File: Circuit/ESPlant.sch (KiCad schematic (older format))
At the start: 43 parts, among them P1 SOIL, P101 CONN_DIGITAL, P102 CONN_ANALOG, P103 CONN_SERIAL, P104 CONN_I2C, P105 SOLAR, P106 USB_5PIN_SHELL, P109 CONN_PWR, P110 CONN_01X05, P111 UV, P112 TEMP, P113 NEOPIXEL, P114 PIR, Q101 FDN340P, SW101 RESET, SW102 PRGM, SW103 RESET, U101 STM32F042F, U103 ESP-12E

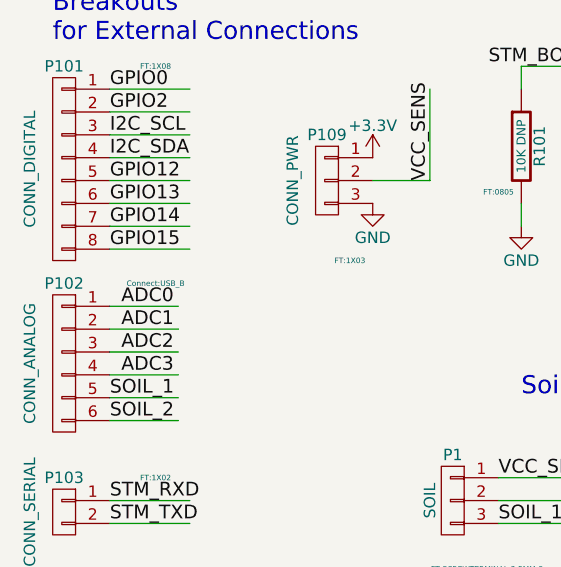
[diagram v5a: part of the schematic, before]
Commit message: First cut routing
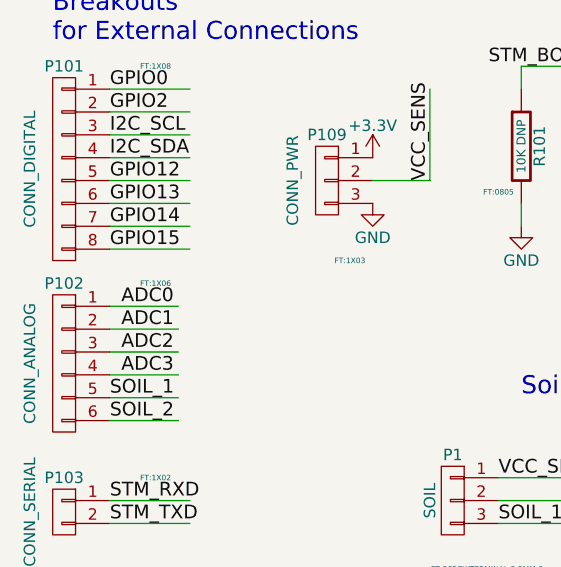
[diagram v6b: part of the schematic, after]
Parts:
- P102: footprint Connect:USB_B -> FT:1X06
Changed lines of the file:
@@
 F 0 "P102" H 750 6300 50  0000 C CNN
 F 1 "CONN_ANALOG" V 900 5950 50  0000 C CNN
-F 2 "Connect:USB_B" H 350 6300 24  0000 C CNN
+F 2 "FT:1X06" H 350 6300 24  0000 C CNN
 F 3 "" H 750 5950 60  0000 C CNN
 	1    750  5950

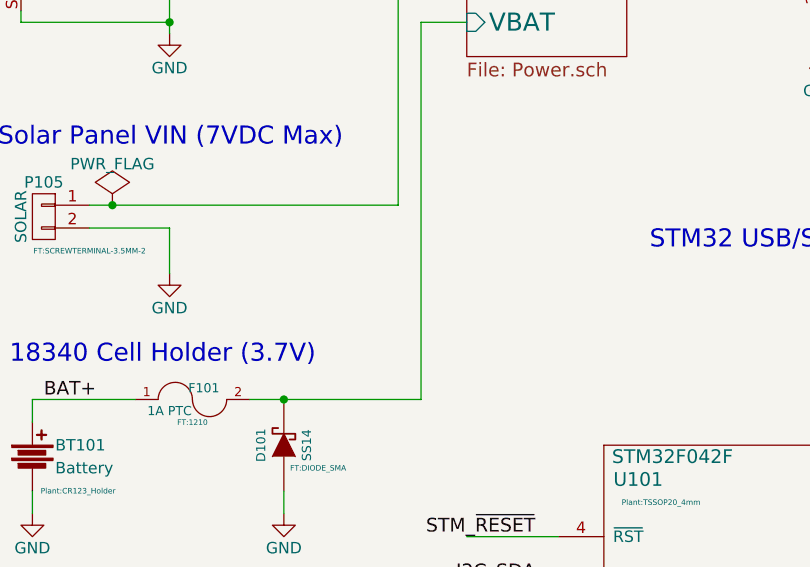
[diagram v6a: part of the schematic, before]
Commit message: Add crowbar diode for solar panel polarity protection
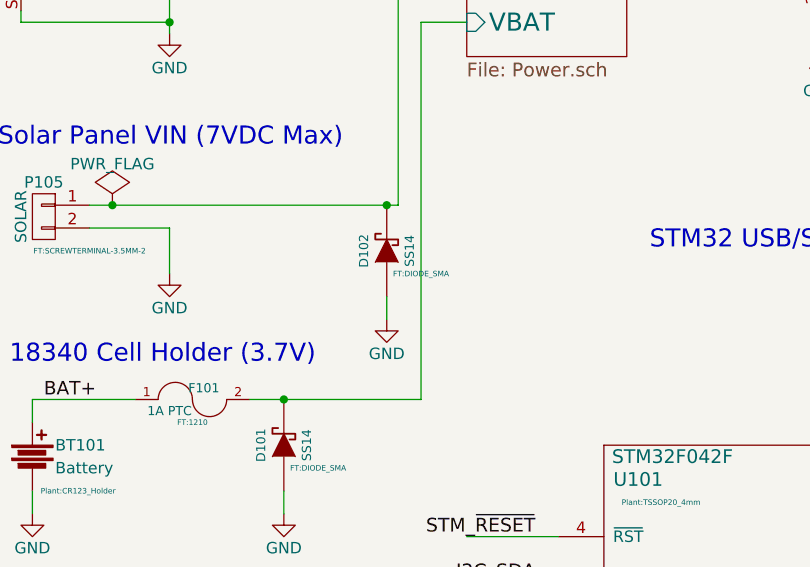
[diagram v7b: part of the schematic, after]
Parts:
- added D102: SS14, FT:DIODE_SMA, symbol DIODE_SCHOTTKY
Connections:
- wire segments 163 -> 164
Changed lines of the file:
@@
 $EndDescr
 $Comp
-L +3.3V #PWR01
+L +3.3V #PWR123
 U 1 1 56375ED2
 P 9250 5800
-F 0 "#PWR01" H 9250 5650 50  0001 C CNN
+F 0 "#PWR123" H 9250 5650 50  0001 C CNN
 F 1 "+3.3V" H 9250 5940 50  0000 C CNN
 F 2 "" H 9250 5800 60  0000 C CNN
@@
 $EndComp
 $Comp
-L GND #PWR02
+L GND #PWR129
 U 1 1 56375FE4
 P 10550 1700
-F 0 "#PWR02" H 10550 1450 50  0001 C CNN
+F 0 "#PWR129" H 10550 1450 50  0001 C CNN
 F 1 "GND" H 10550 1550 50  0000 C CNN
 F 2 "" H 10550 1700 60  0000 C CNN
@@
 $EndComp
 $Comp
-L +3.3V #PWR03
+L +3.3V #PWR128
 U 1 1 56376117
 P 10250 1400
-F 0 "#PWR03" H 10250 1250 50  0001 C CNN
+F 0 "#PWR128" H 10250 1250 50  0001 C CNN
 F 1 "+3.3V" H 10250 1540 50  0000 C CNN
 F 2 "" H 10250 1400 60  0000 C CNN
@@
 $EndComp
 $Comp
-L +3.3V #PWR04
+L +3.3V #PWR117
 U 1 1 5637689F
 P 7000 1800
-F 0 "#PWR04" H 7000 1650 50  0001 C CNN
+F 0 "#PWR117" H 7000 1650 50  0001 C CNN
 F 1 "+3.3V" H 7000 1950 50  0000 C CNN
 F 2 "" H 7000 1800 60  0000 C CNN
@@
 $EndComp
 $Comp
-L GND #PWR05
+L GND #PWR125
 U 1 1 5637692A
 P 9750 1950
-F 0 "#PWR05" H 9750 1700 50  0001 C CNN
+F 0 "#PWR125" H 9750 1700 50  0001 C CNN
 F 1 "GND" V 9750 1750 50  0000 C CNN
 F 2 "" H 9750 1950 60  0000 C CNN
@@
 $EndComp
 $Comp
-L GND #PWR06
+L GND #PWR102
 U 1 1 56377AB6
 P 1450 1600
-F 0 "#PWR06" H 1450 1350 50  0001 C CNN
+F 0 "#PWR102" H 1450 1350 50  0001 C CNN
 F 1 "GND" H 1450 1450 50  0000 C CNN
 F 2 "" H 1450 1600 60  0000 C CNN
@@
 $EndComp
 $Comp
-L GND #PWR07
+L GND #PWR121
 U 1 1 564A2882
 P 8900 6250
-F 0 "#PWR07" H 8900 6000 50  0001 C CNN
+F 0 "#PWR121" H 8900 6000 50  0001 C CNN
 F 1 "GND" H 8900 6100 50  0000 C CNN
 F 2 "" H 8900 6250 60  0000 C CNN
@@
 Solar Panel VIN (7VDC Max)
 $Comp
-L GND #PWR08
+L GND #PWR103
 U 1 1 564B24B3
 P 1450 2650
-F 0 "#PWR08" H 1450 2400 50  0001 C CNN
+F 0 "#PWR103" H 1450 2400 50  0001 C CNN
 F 1 "GND" H 1450 2500 50  0000 C CNN
 F 2 "" H 1450 2650 60  0000 C CNN
@@
 $EndComp
 $Comp
-L +3.3V #PWR09
+L +3.3V #PWR114
 U 1 1 564B2FF9
 P 5250 900
-F 0 "#PWR09" H 5250 750 50  0001 C CNN
+F 0 "#PWR114" H 5250 750 50  0001 C CNN
 F 1 "+3.3V" H 5250 1040 50  0000 C CNN
 F 2 "" H 5250 900 60  0000 C CNN
@@
 $EndComp
 $Comp
-L GND #PWR010
+L GND #PWR110
 U 1 1 564B3125
 P 4300 1700
-F 0 "#PWR010" H 4300 1450 50  0001 C CNN
+F 0 "#PWR110" H 4300 1450 50  0001 C CNN
 F 1 "GND" H 4300 1550 50  0000 C CNN
 F 2 "" H 4300 1700 60  0000 C CNN
@@
 18340 Cell Holder (3.7V)\n
 $Comp
-L GND #PWR011
+L GND #PWR101
 U 1 1 564B5F41
 P 850 3700
-F 0 "#PWR011" H 850 3450 50  0001 C CNN
+F 0 "#PWR101" H 850 3450 50  0001 C CNN
 F 1 "GND" H 850 3550 50  0000 C CNN
 F 2 "" H 850 3700 60  0000 C CNN
@@
 STM_~RESET
 $Comp
-L GND #PWR012
+L GND #PWR127
 U 1 1 564C3A22
 P 10200 5050
-F 0 "#PWR012" H 10200 4800 50  0001 C CNN
+F 0 "#PWR127" H 10200 4800 50  0001 C CNN
 F 1 "GND" H 10200 4900 50  0000 C CNN
 F 2 "" H 10200 5050 60  0000 C CNN
@@
 ESP_~RESET
 $Comp
-L GND #PWR013
+L GND #PWR124
 U 1 1 564C33B9
 P 9600 5050
-F 0 "#PWR013" H 9600 4800 50  0001 C CNN
+F 0 "#PWR124" H 9600 4800 50  0001 C CNN
 F 1 "GND" H 9600 4900 50  0000 C CNN
 F 2 "" H 9600 5050 60  0000 C CNN
@@
 STM_~RESET
 $Comp
-L GND #PWR014
+L GND #PWR130
 U 1 1 564C4984
 P 10700 5050
-F 0 "#PWR014" H 10700 4800 50  0001 C CNN
+F 0 "#PWR130" H 10700 4800 50  0001 C CNN
 F 1 "GND" H 10700 4900 50  0000 C CNN
 F 2 "" H 10700 5050 60  0000 C CNN
@@
 VCC_SENS
 $Comp
-L GND #PWR015
+L GND #PWR108
 U 1 1 564FA125
 P 2650 7350
-F 0 "#PWR015" H 2650 7100 50  0001 C CNN
+F 0 "#PWR108" H 2650 7100 50  0001 C CNN
 F 1 "GND" H 2650 7200 50  0000 C CNN
 F 2 "" H 2650 7350 60  0000 C CNN
@@
 ADC3
 $Comp
-L PWR_FLAG #FLG016
+L PWR_FLAG #FLG101
 U 1 1 5650A161
 P 1200 2350
-F 0 "#FLG016" H 1200 2445 50  0001 C CNN
+F 0 "#FLG101" H 1200 2445 50  0001 C CNN
 F 1 "PWR_FLAG" H 1200 2530 50  0000 C CNN
 F 2 "" H 1200 2350 60  0000 C CNN
@@
 $EndComp
 $Comp
-L GND #PWR017
+L GND #PWR116
 U 1 1 564E839D
 P 6700 5500
-F 0 "#PWR017" H 6700 5250 50  0001 C CNN
+F 0 "#PWR116" H 6700 5250 50  0001 C CNN
 F 1 "GND" H 6700 5350 50  0000 C CNN
 F 2 "" H 6700 5500 60  0000 C CNN
@@
 STM_SWCLK
 $Comp
-L GND #PWR018
+L GND #PWR112
 U 1 1 564EA3B7
 P 4550 5300
-F 0 "#PWR018" H 4550 5050 50  0001 C CNN
+F 0 "#PWR112" H 4550 5050 50  0001 C CNN
 F 1 "GND" H 4550 5150 50  0000 C CNN
 F 2 "" H 4550 5300 60  0000 C CNN
@@
 $EndComp
 $Comp
-L +3.3V #PWR019
+L +3.3V #PWR111
 U 1 1 564EA803
 P 4450 2800
-F 0 "#PWR019" H 4450 2650 50  0001 C CNN
+F 0 "#PWR111" H 4450 2650 50  0001 C CNN
 F 1 "+3.3V" H 4450 2940 50  0000 C CNN
 F 2 "" H 4450 2800 60  0000 C CNN
@@
 $EndComp
 $Comp
-L GND #PWR020
+L GND #PWR109
 U 1 1 564EB5A8
 P 2750 5350
-F 0 "#PWR020" H 2750 5100 50  0001 C CNN
+F 0 "#PWR109" H 2750 5100 50  0001 C CNN
 F 1 "GND" H 2750 5200 50  0000 C CNN
 F 2 "" H 2750 5350 60  0000 C CNN
@@
 $EndComp
 $Comp
-L +3.3V #PWR021
+L +3.3V #PWR118
 U 1 1 564ED1D2
 P 7400 5550
-F 0 "#PWR021" H 7400 5400 50  0001 C CNN
+F 0 "#PWR118" H 7400 5400 50  0001 C CNN
 F 1 "+3.3V" H 7400 5690 50  0000 C CNN
 F 2 "" H 7400 5550 60  0000 C CNN
@@
 $EndComp
 $Comp
-L GND #PWR022
+L GND #PWR119
 U 1 1 564ED428
 P 7400 6100
-F 0 "#PWR022" H 7400 5850 50  0001 C CNN
+F 0 "#PWR119" H 7400 5850 50  0001 C CNN
 F 1 "GND" H 7400 5950 50  0000 C CNN
 F 2 "" H 7400 6100 60  0000 C CNN
@@
 $EndComp
 $Comp
-L GND #PWR023
+L GND #PWR113
 U 1 1 564EE0F6
 P 5150 3250
-F 0 "#PWR023" H 5150 3000 50  0001 C CNN
+F 0 "#PWR113" H 5150 3000 50  0001 C CNN
 F 1 "GND" H 5150 3100 50  0001 C CNN
 F 2 "" H 5150 3250 60  0000 C CNN
@@
 $EndComp
 $Comp
-L GND #PWR024
+L GND #PWR120
 U 1 1 56576EBF
 P 8250 3600
-F 0 "#PWR024" H 8250 3350 50  0001 C CNN
+F 0 "#PWR120" H 8250 3350 50  0001 C CNN
 F 1 "GND" H 8250 3450 50  0000 C CNN
 F 2 "" H 8250 3600 60  0000 C CNN
@@
 $EndComp
 $Comp
-L GND #PWR025
+L GND #PWR131
 U 1 1 5657CEA4
 P 10800 3600
-F 0 "#PWR025" H 10800 3350 50  0001 C CNN
+F 0 "#PWR131" H 10800 3350 50  0001 C CNN
 F 1 "GND" H 10800 3450 50  0000 C CNN
 F 2 "" H 10800 3600 60  0000 C CNN
@@
 $EndComp
 $Comp
-L GND #PWR026
+L GND #PWR122
 U 1 1 5657D68A
 P 9050 3600
-F 0 "#PWR026" H 9050 3350 50  0001 C CNN
+F 0 "#PWR122" H 9050 3350 50  0001 C CNN
 F 1 "GND" H 9050 3450 50  0000 C CNN
 F 2 "" H 9050 3600 60  0000 C CNN
@@
 $EndComp
 $Comp
-L GND #PWR027
+L GND #PWR126
 U 1 1 5657D767
 P 9950 3600
-F 0 "#PWR027" H 9950 3350 50  0001 C CNN
+F 0 "#PWR126" H 9950 3350 50  0001 C CNN
 F 1 "GND" H 9950 3450 50  0000 C CNN
 F 2 "" H 9950 3600 60  0000 C CNN
@@
 $EndComp
 $Comp
-L +3.3V #PWR028
+L +3.3V #PWR115
 U 1 1 56596CF8
 P 6550 2350
-F 0 "#PWR028" H 6550 2200 50  0001 C CNN
+F 0 "#PWR115" H 6550 2200 50  0001 C CNN
 F 1 "+3.3V" H 6550 2490 50  0000 C CNN
 F 2 "" H 6550 2350 60  0000 C CNN
@@
 $EndComp
 $Comp
-L +3.3V #PWR029
+L +3.3V #PWR105
 U 1 1 565C1114
 P 2100 5050
-F 0 "#PWR029" H 2100 4900 50  0001 C CNN
+F 0 "#PWR105" H 2100 4900 50  0001 C CNN
 F 1 "+3.3V" H 2100 5190 50  0000 C CNN
 F 2 "" H 2100 5050 60  0000 C CNN
@@
 $EndComp
 $Comp
-L GND #PWR030
+L GND #PWR106
 U 1 1 565C1810
 P 2100 5250
-F 0 "#PWR030" H 2100 5000 50  0001 C CNN
+F 0 "#PWR106" H 2100 5000 50  0001 C CNN
 F 1 "GND" H 2100 5100 50  0000 C CNN
 F 2 "" H 2100 5250 60  0000 C CNN
@@
 $EndComp
 $Comp
-L GND #PWR031
+L GND #PWR104
 U 1 1 565D25EB
 P 1950 3700
-F 0 "#PWR031" H 1950 3450 50  0001 C CNN
+F 0 "#PWR104" H 1950 3450 50  0001 C CNN
 F 1 "GND" H 1950 3550 50  0000 C CNN
 F 2 "" H 1950 3700 60  0000 C CNN
@@
 GPIO14
 Connection ~ 1950 3200
+$Comp
+L DIODE_SCHOTTKY D102
+U 1 1 565BCCC2
+P 2400 2550
+F 0 "D102" H 2400 2650 40  0000 C CNN
+F 1 "SS14" H 2400 2450 40  0000 C CNN
+F 2 "FT:DIODE_SMA" V 2300 2400 24  0000 C CNN
+F 3 "" H 2400 2550 60  0000 C CNN
+	1    2400 2550
+	0    -1   -1   0
+$EndComp
+$Comp
+L GND #PWR107
+U 1 1 565BCCC8
+P 2400 2850
+F 0 "#PWR107" H 2400 2600 50  0001 C CNN
+F 1 "GND" H 2400 2700 50  0000 C CNN
+F 2 "" H 2400 2850 60  0000 C CNN
+F 3 "" H 2400 2850 60  0000 C CNN
+	1    2400 2850
+	1    0    0    -1
+$EndComp
+Wire Wire Line
+	2400 2750 2400 2850
+Connection ~ 2400 2350
 $EndSCHEMATC

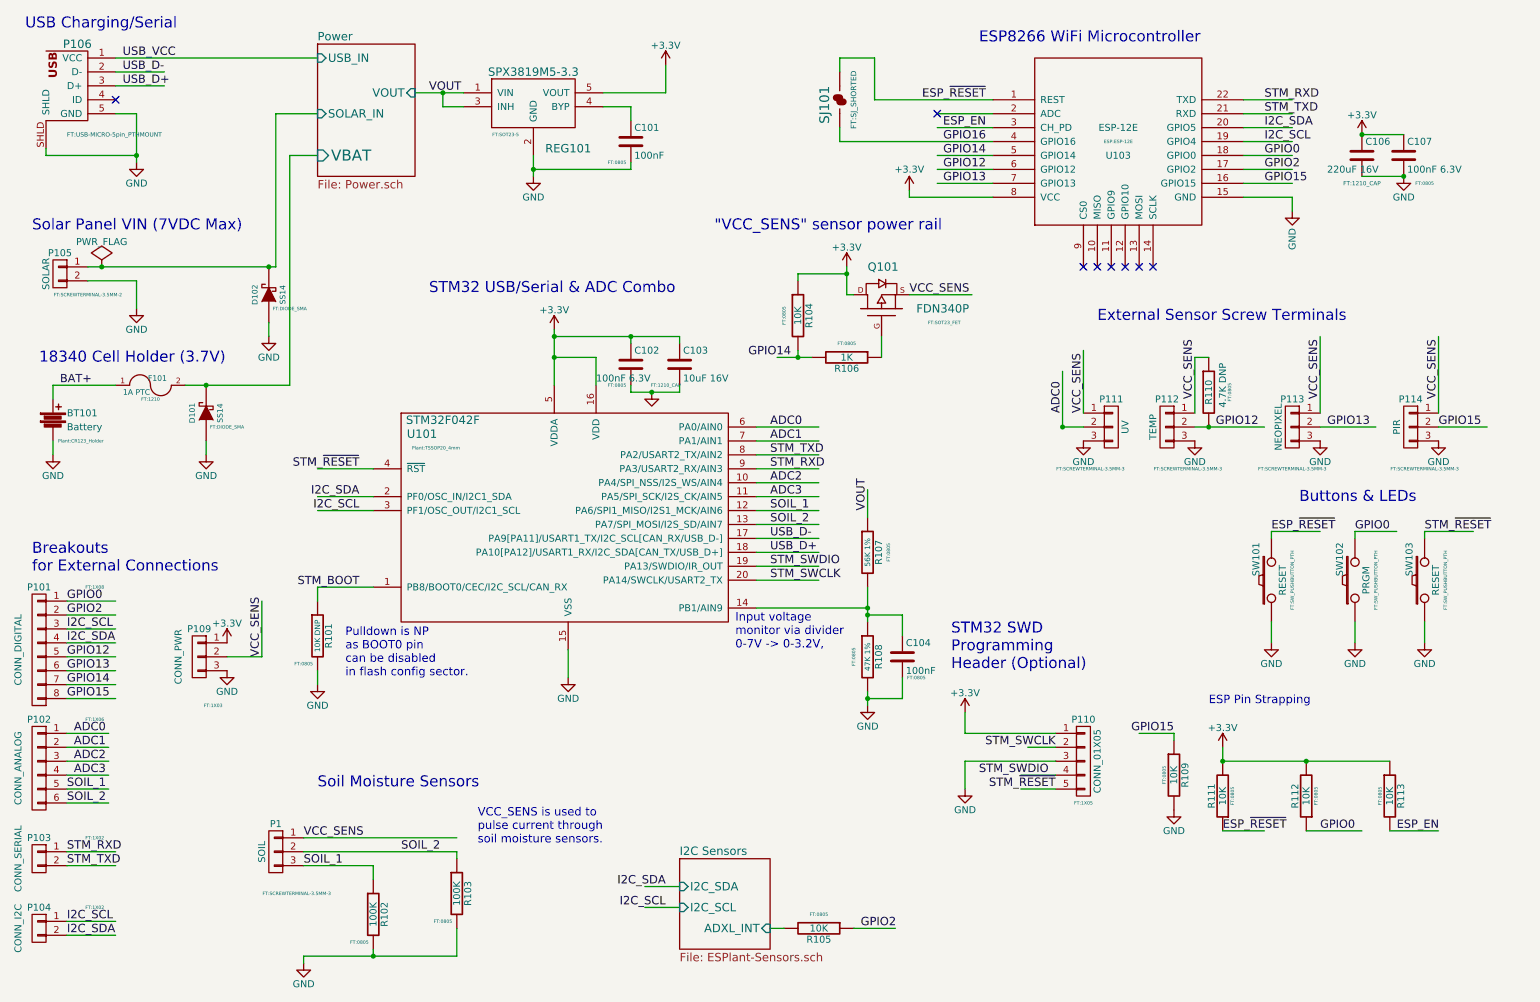
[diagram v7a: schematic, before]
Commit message: Revise schematic for V1.1 based on V1.0 evaluation:
* Swap SDA, SCL on ESP (5,4 to 4,5) to match Arduino default
* Q101 source, drain were swapped
* BME280 change i2c address config  0x76 -> 0x77 (match Adafruit library)
* ADXL345 change i2c address from 0x1d -> 0x53 (match Adafruit library)
* Specify colours for "charging", "done" LEDs in component values
* R202, R203 LED series resistors changed to 1K
* Add GPIO2 pullup to strapping resistors, required for reliable reset
* Add autoreset: connect ESP_RESET to PA7 on STM32, GPIO0 to PB8. Remove
  "ADC5" pin from design.
* Add 1K series resistor between GPIO16 and RESET (replacing solder
  jumper). Otherwise pulling reset line draws >50mA!!
* Add 1K series resistor from GPIO0 to GPIO0 reset button & STM32
  GPIO. This is because GPIO0 defaults to clock output on reset,
  driving a square wave.
* Change 220uF 1210 bulk capacitor value to 100uF, reflecting part
  availability and reliability shown in testing.
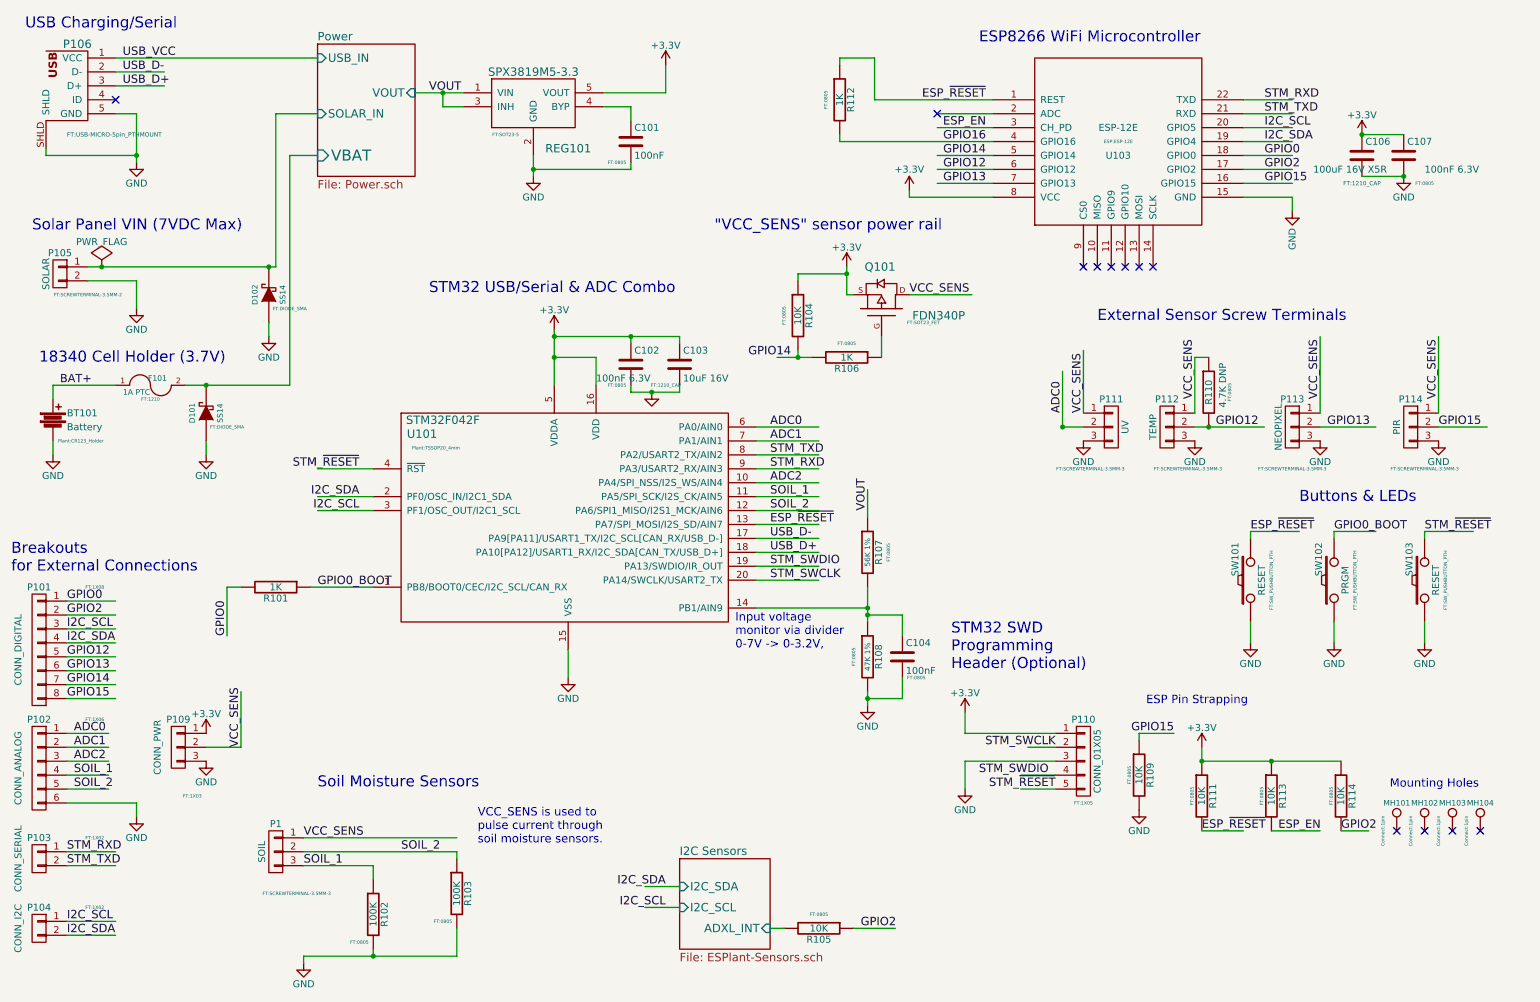
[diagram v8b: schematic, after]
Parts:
- removed SJ101: SJ, FT:SJ_SHORTED, symbol SJ
- added MH101, MH102, MH103, MH104: TEST_1P, Connect:1pin, symbol TEST_1P
- added R114: 10K, FT:0805, symbol R
- C106: value 220uF 16V -> 100uF 16V X5R
- R101: value 10K DNP -> 1K; footprint FT:0805 -> (none)
- R112: value 10K -> 1K
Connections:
- net labels added: GPIO0_BOOT
- net labels removed: ADC3, STM_BOOT
- wire segments 164 -> 165
- no-connect marks 8 -> 12
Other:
- note added: "Mounting Holes\n"
- note removed: "Pulldown is NP\nas BOOT0 pin\ncan be disabled\nin flash config sector."
- moved on the sheet: P109, R109, R113, SW101, SW102
